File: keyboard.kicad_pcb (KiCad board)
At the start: 2 copper layers, 69.1 x 68.1 mm, 78 parts, among them CON1 USB-MICRO-B, J1 CONN-PALM-FOLD-KB, P1 Keyboard Even, P2 Keyboard Odd, P3 PS2, P4 Palm Serial, P5 ARM debug header, P6 Power, P7 USB_H, Q1 BSS138, Q2 BSS138, Q3 BSS138, SW1 SW_PUSH, U1 CONN-X220-KB, U2 MCP1700-2202E/TT, U3 EFM32G222F32, X1 CRYSTAL

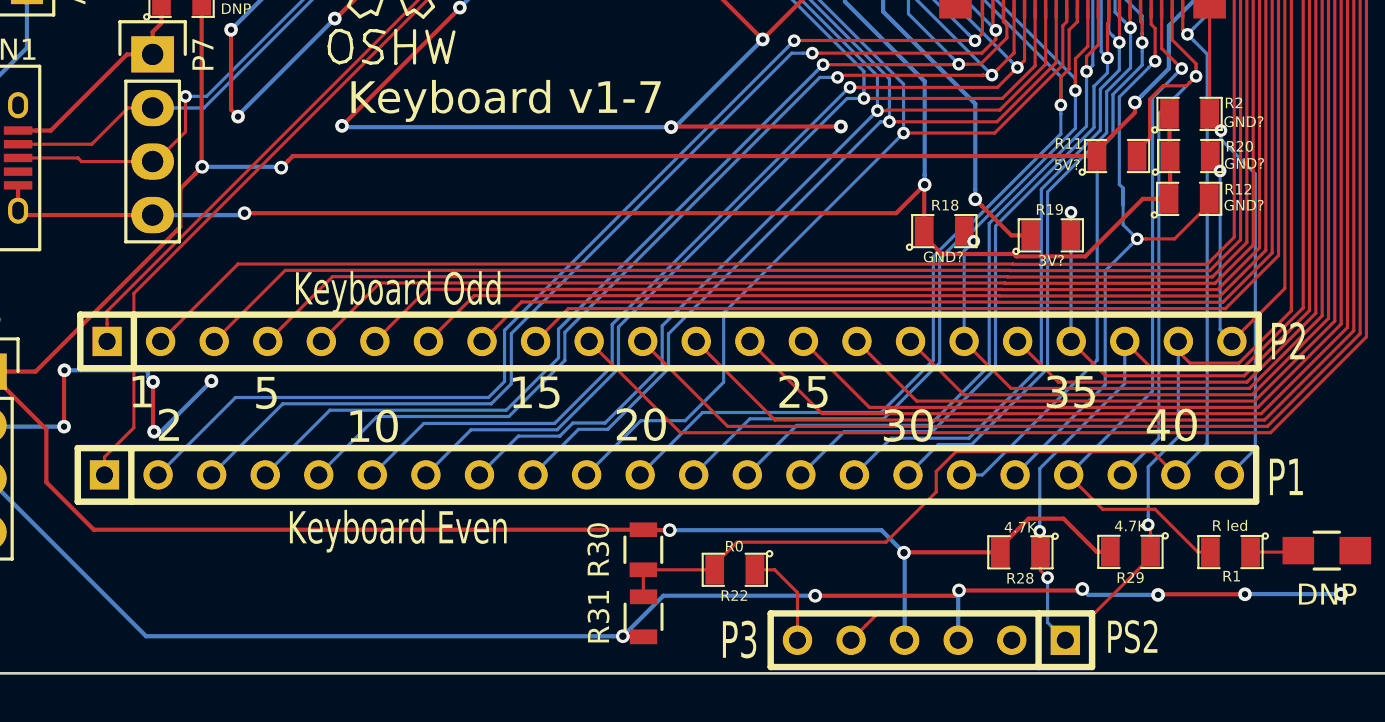
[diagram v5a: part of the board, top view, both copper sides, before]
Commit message: Add pin some labels to silkscreen
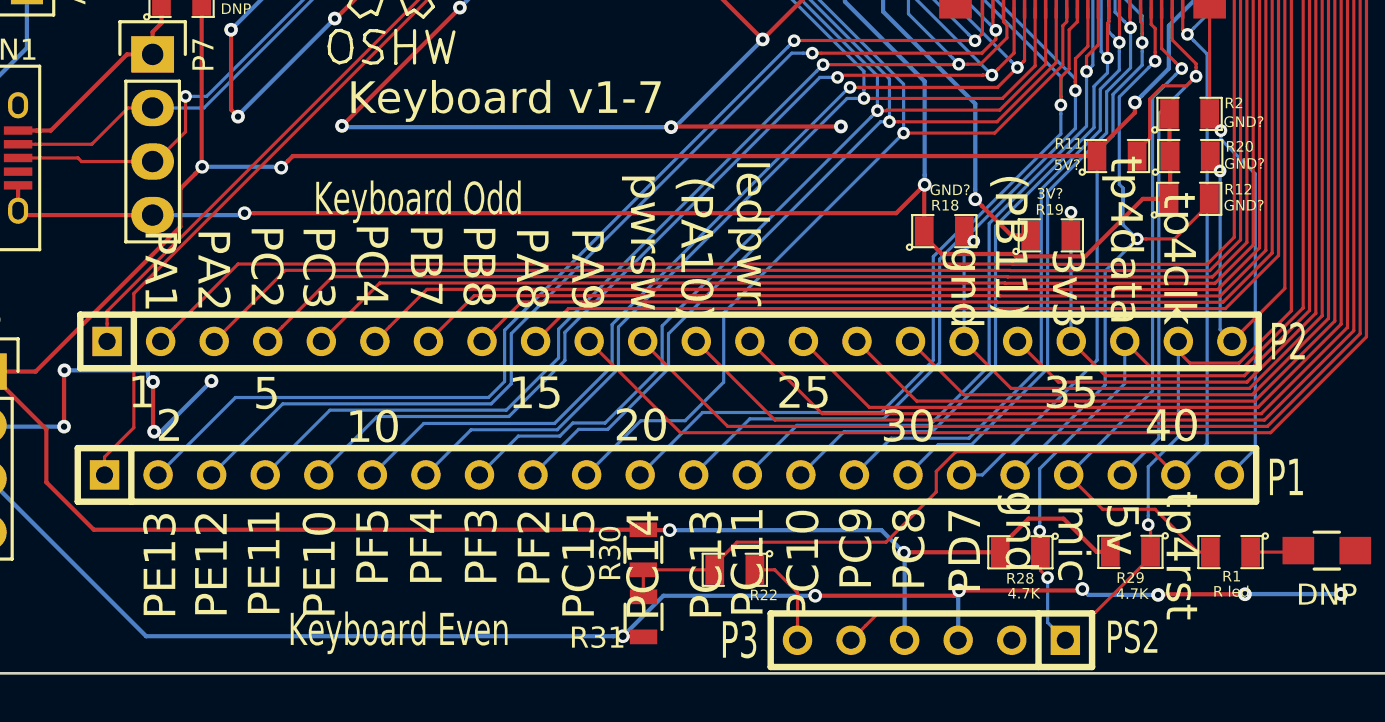
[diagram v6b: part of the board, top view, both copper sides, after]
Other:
- board text added: "(PA10)"
- board text added: "(PB11)"
- board text added: "3v3"
- board text added: "5v"
- board text added: "PA1"
- board text added: "PA2"
- board text added: "PA8"
- board text added: "PA9"
- board text added: "PB7"
- board text added: "PB8"
- board text added: "PC10"
- board text added: "PC11"
- board text added: "PC13"
- board text added: "PC14"
- board text added: "PC15"
- board text added: "PC2"
- board text added: "PC3"
- board text added: "PC4"
- board text added: "PC8"
- board text added: "PC9"
- board text added: "PD7"
- board text added: "PE10"
- board text added: "PE11"
- board text added: "PE12"
- board text added: "PE13"
- board text added: "PF2"
- board text added: "PF3"
- board text added: "PF4"
- board text added: "PF5"
- board text added: "gnd"
- board text added: "ledpwr"
- board text added: "mic"
- board text added: "pwrsw"
- board text added: "tp4clk"
- board text added: "tp4data"
- board text added: "tp4rst"
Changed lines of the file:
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@@
     (area 102.441666 17.2128 214.297165 118.337754)
     (thickness 1.6)
-    (drawings 51)
+    (drawings 88)
     (tracks 2359)
     (zones 0)
@@
     (40 Dwgs.User user hide)
     (41 Cmts.User user hide)
-    (42 Eco1.User user hide)
+    (42 Eco1.User user)
     (43 Eco2.User user hide)
     (44 Edge.Cuts user)
@@
     (at 168.2175 106.18 180)
     (attr smd)
-    (fp_text reference R22 (at 0.0175 -1.24 180) (layer F.SilkS)
-      (effects (font (size 0.50038 0.50038) (thickness 0.10922)))
-    )
-    (fp_text value R0 (at 0.0275 1.1 180) (layer F.SilkS)
+    (fp_text reference R22 (at -1.3725 -1.21 180) (layer F.SilkS)
+      (effects (font (size 0.50038 0.50038) (thickness 0.10922)))
+    )
+    (fp_text value R0 (at -0.1125 -6.08 180) (layer Eco1.User)
       (effects (font (size 0.50038 0.50038) (thickness 0.10922)))
     )
@@
       (effects (font (size 1.72974 1.08712) (thickness 0.27178)))
     )
-    (fp_text value "Keyboard Odd" (at -17.95 -2.46 180) (layer F.SilkS)
+    (fp_text value "Keyboard Odd" (at -16.99 -6.75 180) (layer F.SilkS)
       (effects (font (size 1.524 1.016) (thickness 0.254)))
     )
@@
       (effects (font (size 1.72974 1.08712) (thickness 0.27178)))
     )
-    (fp_text value "Keyboard Even" (at -17.83 2.54 180) (layer F.SilkS)
+    (fp_text value "Keyboard Even" (at -17.79 7.36 180) (layer F.SilkS)
       (effects (font (size 1.524 1.016) (thickness 0.254)))
     )
@@
       (effects (font (size 0.50038 0.50038) (thickness 0.10922)))
     )
-    (fp_text value "R led" (at 0.0225 1.24 180) (layer F.SilkS)
+    (fp_text value "R led" (at -0.0375 -1.88 180) (layer F.SilkS)
       (effects (font (size 0.50038 0.50038) (thickness 0.10922)))
     )
@@
       (effects (font (size 0.50038 0.50038) (thickness 0.10922)))
     )
-    (fp_text value GND? (at -0.0425 1.24) (layer F.SilkS)
+    (fp_text value GND? (at 0.2775 -1.94) (layer F.SilkS)
       (effects (font (size 0.50038 0.50038) (thickness 0.10922)))
     )
@@
       (effects (font (size 0.50038 0.50038) (thickness 0.10922)))
     )
-    (fp_text value 3V? (at 0.0275 1.21) (layer F.SilkS)
+    (fp_text value 3V? (at -0.0425 -1.97) (layer F.SilkS)
       (effects (font (size 0.50038 0.50038) (thickness 0.10922)))
     )
@@
       (effects (font (size 0.50038 0.50038) (thickness 0.10922)))
     )
-    (fp_text value 4.7K (at -0.0025 1.21 180) (layer F.SilkS)
+    (fp_text value 4.7K (at -0.0825 -2 180) (layer F.SilkS)
       (effects (font (size 0.50038 0.50038) (thickness 0.10922)))
     )
@@
       (effects (font (size 0.50038 0.50038) (thickness 0.10922)))
     )
-    (fp_text value 4.7K (at 0.01 1.17 180) (layer F.SilkS)
+    (fp_text value 4.7K (at -0.16 -1.96 180) (layer F.SilkS)
       (effects (font (size 0.50038 0.50038) (thickness 0.10922)))
     )
@@
     (tags "resistor 0805")
     (attr smd)
-    (fp_text reference R30 (at 0 -2.1 90) (layer F.SilkS)
+    (fp_text reference R30 (at -0.17 -1.56 90) (layer F.SilkS)
       (effects (font (size 1 1) (thickness 0.15)))
     )
-    (fp_text value DNP (at 0 2.1 90) (layer F.Fab)
+    (fp_text value DNP (at -0.11 1.41 90) (layer F.Fab)
       (effects (font (size 1 1) (thickness 0.15)))
     )
@@
     (tags "resistor 0805")
     (attr smd)
-    (fp_text reference R31 (at 0 -2.1 90) (layer F.SilkS)
+    (fp_text reference R31 (at -1 -2.18 180) (layer F.SilkS)
       (effects (font (size 1 1) (thickness 0.15)))
     )
-    (fp_text value DNP (at 0 2.1 90) (layer F.Fab)
+    (fp_text value DNP (at 0.01 1.45 90) (layer F.Fab)
       (effects (font (size 1 1) (thickness 0.15)))
     )
@@
       (net 12 GND))
   )
+  (gr_text pwrsw (at 163.99 90.64 270) (layer F.SilkS)
+    (effects (font (size 1.5 1.5) (thickness 0.15)))
+  )
+  (gr_text tp4rst (at 189.39 105.51 270) (layer F.SilkS)
+    (effects (font (size 1.5 1.5) (thickness 0.15)))
+  )
+  (gr_text 5v (at 186.57 104.26 270) (layer F.SilkS)
+    (effects (font (size 1.5 1.5) (thickness 0.15)))
+  )
+  (gr_text mic (at 184.26 104.94 270) (layer F.SilkS)
+    (effects (font (size 1.5 1.5) (thickness 0.15)))
+  )
+  (gr_text gnd (at 181.78 104.37 270) (layer F.SilkS)
+    (effects (font (size 1.5 1.5) (thickness 0.15)))
+  )
+  (gr_text tp4clk (at 189.28 91.42 270) (layer F.SilkS)
+    (effects (font (size 1.5 1.5) (thickness 0.15)))
+  )
+  (gr_text tp4data (at 186.76 90.56 270) (layer F.SilkS)
+    (effects (font (size 1.5 1.5) (thickness 0.15)))
+  )
+  (gr_text 3v3 (at 184 92.84 270) (layer F.SilkS)
+    (effects (font (size 1.5 1.5) (thickness 0.15)))
+  )
+  (gr_text gnd (at 179.18 92.8 270) (layer F.SilkS)
+    (effects (font (size 1.5 1.5) (thickness 0.15)))
+  )
+  (gr_text ledpwr (at 169.02 90.2 270) (layer F.SilkS)
+    (effects (font (size 1.5 1.5) (thickness 0.15)))
+  )
+  (gr_text "(PA10)" (at 166.38 90.93 270) (layer F.SilkS)
+    (effects (font (size 1.5 1.5) (thickness 0.15)))
+  )
+  (gr_text PA1 (at 140.97 92 270) (layer F.SilkS)
+    (effects (font (size 1.5 1.5) (thickness 0.15)))
+  )
+  (gr_text PA2 (at 143.48 91.97 270) (layer F.SilkS)
+    (effects (font (size 1.5 1.5) (thickness 0.15)))
+  )
+  (gr_text PA8 (at 158.58 91.9 270) (layer F.SilkS)
+    (effects (font (size 1.5 1.5) (thickness 0.15)))
+  )
+  (gr_text PA9 (at 161.2 91.92 270) (layer F.SilkS)
+    (effects (font (size 1.5 1.5) (thickness 0.15)))
+  )
+  (gr_text PB7 (at 153.55 91.77 270) (layer F.SilkS)
+    (effects (font (size 1.5 1.5) (thickness 0.15)))
+  )
+  (gr_text PB8 (at 156.06 91.79 270) (layer F.SilkS)
+    (effects (font (size 1.5 1.5) (thickness 0.15)))
+  )
+  (gr_text "(PB11)" (at 181.29 90.81 270) (layer F.SilkS)
+    (effects (font (size 1.5 1.5) (thickness 0.15)))
+  )
+  (gr_text PC2 (at 146 91.82 270) (layer F.SilkS)
+    (effects (font (size 1.5 1.5) (thickness 0.15)))
+  )
+  (gr_text PC3 (at 148.46 91.85 270) (layer F.SilkS)
+    (effects (font (size 1.5 1.5) (thickness 0.15)))
+  )
+  (gr_text PC4 (at 150.98 91.74 270) (layer F.SilkS)
+    (effects (font (size 1.5 1.5) (thickness 0.15)))
+  )
+  (gr_text PC8 (at 176.5 105.19 90) (layer F.SilkS)
+    (effects (font (size 1.5 1.5) (thickness 0.15)))
+  )
+  (gr_text PC9 (at 173.98 105.17 90) (layer F.SilkS)
+    (effects (font (size 1.5 1.5) (thickness 0.15)))
+  )
+  (gr_text PC10 (at 171.47 105.89 90) (layer F.SilkS)
+    (effects (font (size 1.5 1.5) (thickness 0.15)))
+  )
+  (gr_text PC11 (at 168.84 105.81 90) (layer F.SilkS)
+    (effects (font (size 1.5 1.5) (thickness 0.15)))
+  )
+  (gr_text PC13 (at 166.88 105.94 90) (layer F.SilkS)
+    (effects (font (size 1.5 1.5) (thickness 0.15)))
+  )
+  (gr_text PC14 (at 163.89 105.96 90) (layer F.SilkS)
+    (effects (font (size 1.5 1.5) (thickness 0.15)))
+  )
+  (gr_text PC15 (at 160.84 105.9 90) (layer F.SilkS)
+    (effects (font (size 1.5 1.5) (thickness 0.15)))
+  )
+  (gr_text PD7 (at 179.15 105.28 90) (layer F.SilkS)
+    (effects (font (size 1.5 1.5) (thickness 0.15)))
+  )
+  (gr_text PE10 (at 148.55 105.93 90) (layer F.SilkS)
+    (effects (font (size 1.5 1.5) (thickness 0.15)))
+  )
+  (gr_text PE11 (at 145.93 105.85 90) (layer F.SilkS)
+    (effects (font (size 1.5 1.5) (thickness 0.15)))
+  )
+  (gr_text PE12 (at 143.43 105.91 90) (layer F.SilkS)
+    (effects (font (size 1.5 1.5) (thickness 0.15)))
+  )
+  (gr_text PE13 (at 140.99 105.95 90) (layer F.SilkS)
+    (effects (font (size 1.5 1.5) (thickness 0.15)))
+  )
+  (gr_text PF2 (at 158.73 105.12 90) (layer F.SilkS)
+    (effects (font (size 1.5 1.5) (thickness 0.15)))
+  )
+  (gr_text PF3 (at 156.22 105.09 90) (layer F.SilkS)
+    (effects (font (size 1.5 1.5) (thickness 0.15)))
+  )
+  (gr_text PF4 (at 153.62 105.09 90) (layer F.SilkS)
+    (effects (font (size 1.5 1.5) (thickness 0.15)))
+  )
+  (gr_text PF5 (at 151.07 105.09 90) (layer F.SilkS)
+    (effects (font (size 1.5 1.5) (thickness 0.15)))
+  )
   (dimension 68.090018 (width 0.3) (layer Eco1.User)

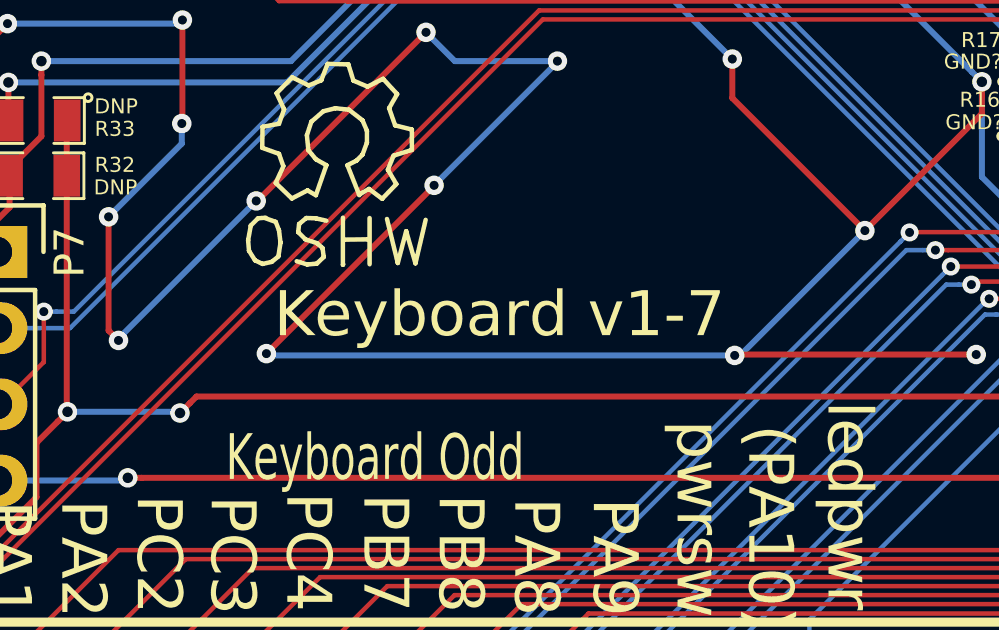
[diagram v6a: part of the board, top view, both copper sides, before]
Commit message: Bump version number on board
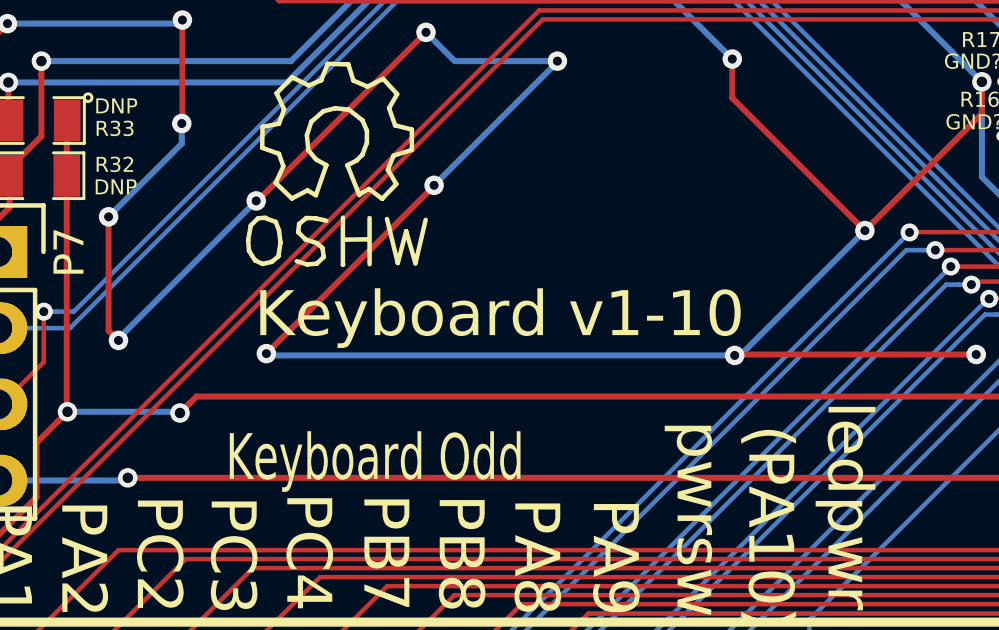
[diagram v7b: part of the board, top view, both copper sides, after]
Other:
- board text added: "Keyboard v1-10"
- board text removed: "Keyboard v1-7"

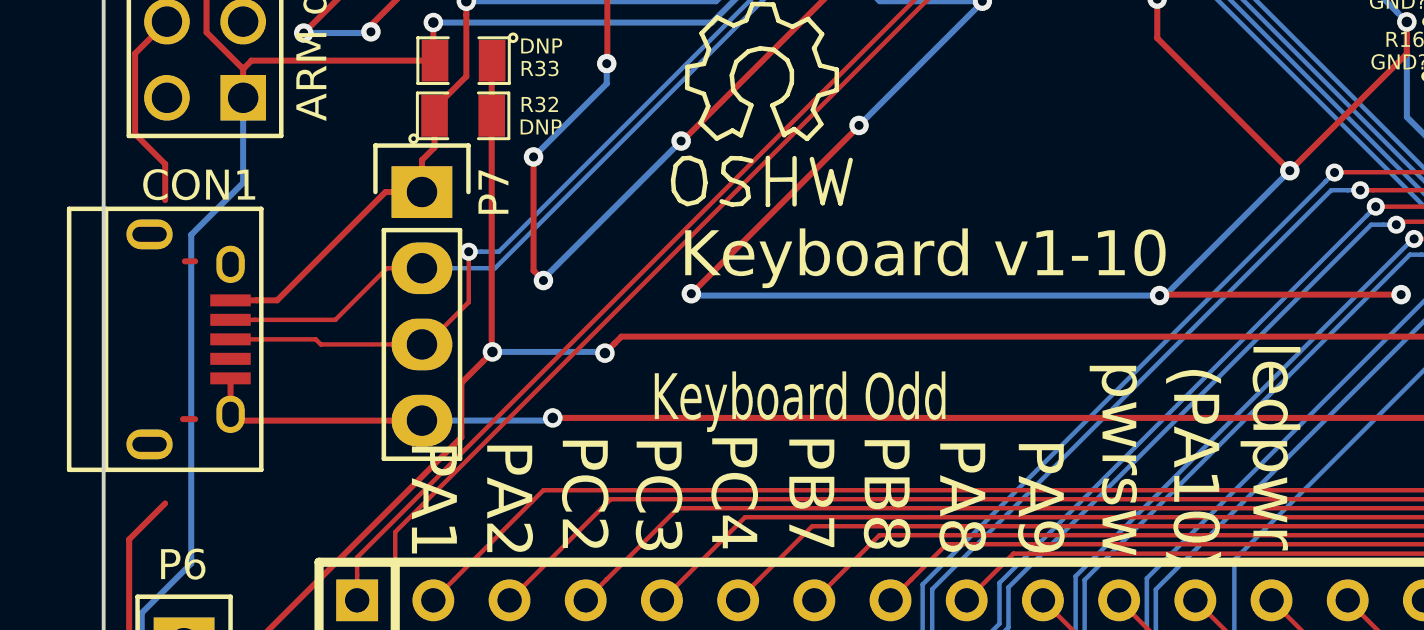
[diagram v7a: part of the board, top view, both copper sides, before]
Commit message: Fix extra traces under microsd
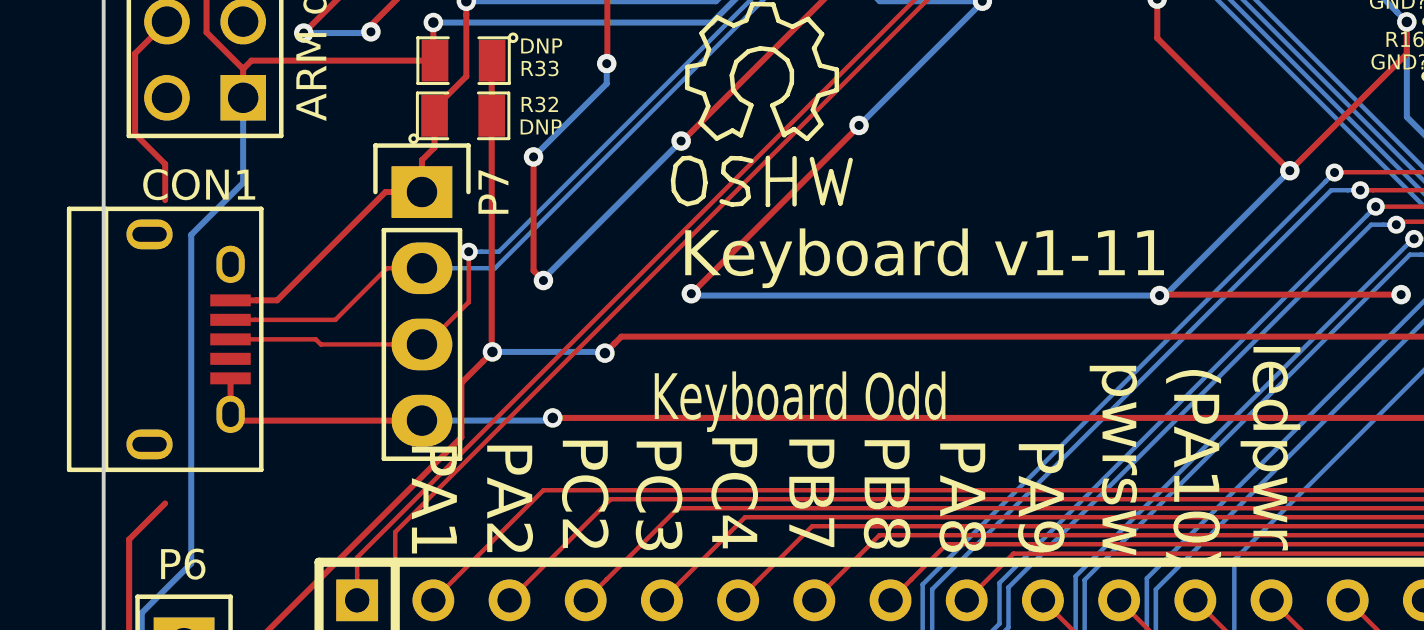
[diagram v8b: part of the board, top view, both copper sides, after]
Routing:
- net (no net): track 0.75 -> 0.00 mm
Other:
- board text added: "Keyboard v1-11"
- board text removed: "Keyboard v1-10"
